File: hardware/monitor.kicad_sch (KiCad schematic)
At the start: 1 part, among them U36 Teensy++2.0

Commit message: Snapshot ep 24 work
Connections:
- net ~{A16} renamed A16
- net ~{A17} renamed A17
- net ~{A18} renamed A18
- net ~{A19} renamed A19
- net ~{A20} renamed A20
- net ~{A21} renamed A21
- net ~{A22} renamed A22
- net ~{A23} renamed A23
- net ~{CLK_EN} renamed ~{CLK_EN_OUT}
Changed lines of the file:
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@@
   (title_block
     (title "Monitor Module")
-    (date "2022-05-23")
-    (rev "A.23")
+    (date "2022-07-04")
+    (rev "A.24")
     (comment 2 "https://github.com/adrienkohlbecker/65C816")
     (comment 3 "Licensed under CERN-OHL-W v2")
@@
     (stroke (width 0) (type default) (color 0 0 0 0))
   )
-  (wire (pts (xy 119.38 83.82) (xy 128.27 83.82))
+  (wire (pts (xy 113.03 83.82) (xy 128.27 83.82))
     (stroke (width 0) (type default) (color 0 0 0 0))
   )
@@
     (effects (font (size 1.27 1.27)) (justify right bottom))
   )
+  (label "A18" (at 175.26 76.2 180)
+    (effects (font (size 1.27 1.27)) (justify right bottom))
+  )
   (label "A3" (at 175.26 124.46 180)
     (effects (font (size 1.27 1.27)) (justify right bottom))
@@
     (effects (font (size 1.27 1.27)) (justify left bottom))
   )
-  (label "{ADDRESS}" (at 86.36 46.99 0)
+  (label "A[0..23]" (at 86.36 46.99 0)
     (effects (font (size 1.27 1.27)) (justify left bottom))
   )
@@
     (effects (font (size 1.27 1.27)) (justify right bottom))
   )
-  (label "~{A16}" (at 171.45 81.28 0)
-    (effects (font (size 1.27 1.27)) (justify left bottom))
-  )
-  (label "~{A20}" (at 171.45 71.12 0)
-    (effects (font (size 1.27 1.27)) (justify left bottom))
-  )
   (label "VA" (at 48.26 33.02 180)
     (effects (font (size 1.27 1.27)) (justify right bottom))
   )
-  (label "~{A23}" (at 121.92 66.04 0)
-    (effects (font (size 1.27 1.27)) (justify left bottom))
+  (label "A17" (at 175.26 78.74 180)
+    (effects (font (size 1.27 1.27)) (justify right bottom))
   )
   (label "D0" (at 121.92 93.98 0)
     (effects (font (size 1.27 1.27)) (justify left bottom))
   )
-  (label "~{A21}" (at 171.45 68.58 0)
-    (effects (font (size 1.27 1.27)) (justify left bottom))
+  (label "A16" (at 175.26 81.28 180)
+    (effects (font (size 1.27 1.27)) (justify right bottom))
   )
   (label "A1" (at 175.26 119.38 180)
     (effects (font (size 1.27 1.27)) (justify right bottom))
   )
-  (label "~{CLK_EN}" (at 52.07 25.4 0)
+  (label "A19" (at 175.26 73.66 180)
+    (effects (font (size 1.27 1.27)) (justify right bottom))
+  )
+  (label "~{CLK_EN_OUT}" (at 52.07 25.4 0)
     (effects (font (size 1.27 1.27)) (justify left bottom))
   )
@@
     (effects (font (size 1.27 1.27)) (justify left bottom))
   )
-  (label "~{CLK_EN}" (at 119.38 83.82 0)
+  (label "~{CLK_EN_OUT}" (at 113.03 83.82 0)
     (effects (font (size 1.27 1.27)) (justify left bottom))
   )
@@
     (effects (font (size 1.27 1.27)) (justify left bottom))
   )
-  (label "{ADDRESS}" (at 48.26 39.37 180)
+  (label "A[0..23]" (at 48.26 39.37 180)
     (effects (font (size 1.27 1.27)) (justify right bottom))
   )
@@
     (effects (font (size 1.27 1.27)) (justify left bottom))
   )
-  (label "~{A18}" (at 171.45 76.2 0)
-    (effects (font (size 1.27 1.27)) (justify left bottom))
-  )
   (label "A14" (at 171.45 109.22 0)
     (effects (font (size 1.27 1.27)) (justify left bottom))
   )
-  (label "SYNC" (at 121.92 91.44 0)
-    (effects (font (size 1.27 1.27)) (justify left bottom))
-  )
-  (label "~{A22}" (at 171.45 66.04 0)
-    (effects (font (size 1.27 1.27)) (justify left bottom))
+  (label "A22" (at 175.26 66.04 180)
+    (effects (font (size 1.27 1.27)) (justify right bottom))
   )
-  (label "~{A19}" (at 171.45 73.66 0)
+  (label "SYNC" (at 121.92 91.44 0)
     (effects (font (size 1.27 1.27)) (justify left bottom))
   )
@@
     (effects (font (size 1.27 1.27)) (justify left bottom))
   )
+  (label "A21" (at 175.26 68.58 180)
+    (effects (font (size 1.27 1.27)) (justify right bottom))
+  )
   (label "CLK_IN" (at 175.26 86.36 180)
     (effects (font (size 1.27 1.27)) (justify right bottom))
@@
     (effects (font (size 1.27 1.27)) (justify left bottom))
   )
+  (label "A23" (at 121.92 66.04 0)
+    (effects (font (size 1.27 1.27)) (justify left bottom))
+  )
   (label "D[0..7]" (at 86.36 133.35 0)
     (effects (font (size 1.27 1.27)) (justify left bottom))
@@
     (effects (font (size 1.27 1.27)) (justify right bottom))
   )
-  (label "~{A17}" (at 171.45 78.74 0)
-    (effects (font (size 1.27 1.27)) (justify left bottom))
+  (label "A20" (at 175.26 71.12 180)
+    (effects (font (size 1.27 1.27)) (justify right bottom))
   )
-  (hierarchical_label "~{CLK_EN}" (shape output) (at 67.31 25.4 0)
+  (hierarchical_label "~{CLK_EN_OUT}" (shape output) (at 67.31 25.4 0)
     (effects (font (size 1.27 1.27)) (justify left))
   )
@@
     (effects (font (size 1.27 1.27)) (justify right))
   )
-  (hierarchical_label "{ADDRESS}" (shape input) (at 33.02 39.37 180)
+  (hierarchical_label "A[0..23]" (shape input) (at 33.02 39.37 180)
     (effects (font (size 1.27 1.27)) (justify right))
   )
@@
       (effects (font (size 1.524 1.524)) (justify left) hide)
     )
-    (property "Datasheet" "" (id 3) (at 148.59 114.3 0)
-      (effects (font (size 1.524 1.524)))
+    (property "Datasheet" "https://www.pjrc.com/store/teensypp.html" (id 3) (at 148.59 114.3 0)
+      (effects (font (size 1.524 1.524)) hide)
     )
     (pin "1")

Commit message: More updates
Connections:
- net CLK_IN renamed CLK_SRC

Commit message: Updates for episode 25
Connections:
- net CLK_SRC renamed CLK_IN
- net ~{CLK_EN_OUT} renamed ~{CLK_EN}
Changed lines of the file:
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@@
   (title_block
     (title "Monitor Module")
-    (date "2022-07-04")
-    (rev "A.24")
+    (date "2022-07-28")
+    (rev "A.25")
     (comment 2 "https://github.com/adrienkohlbecker/65C816")
     (comment 3 "Licensed under CERN-OHL-W v2")
@@
     (stroke (width 0) (type default) (color 0 0 0 0))
   )
-  (wire (pts (xy 113.03 83.82) (xy 128.27 83.82))
+  (wire (pts (xy 119.38 83.82) (xy 128.27 83.82))
     (stroke (width 0) (type default) (color 0 0 0 0))
   )
@@
     (effects (font (size 1.27 1.27)) (justify right bottom))
   )
-  (label "~{CLK_EN_OUT}" (at 52.07 25.4 0)
+  (label "~{CLK_EN}" (at 52.07 25.4 0)
     (effects (font (size 1.27 1.27)) (justify left bottom))
   )
@@
     (effects (font (size 1.27 1.27)) (justify left bottom))
   )
-  (label "~{CLK_EN_OUT}" (at 113.03 83.82 0)
+  (label "~{CLK_EN}" (at 119.38 83.82 0)
     (effects (font (size 1.27 1.27)) (justify left bottom))
   )
@@
     (effects (font (size 1.27 1.27)) (justify right bottom))
   )
-  (label "CLK_SRC" (at 52.07 29.21 0)
+  (label "CLK_IN" (at 52.07 29.21 0)
     (effects (font (size 1.27 1.27)) (justify left bottom))
   )
@@
     (effects (font (size 1.27 1.27)) (justify right bottom))
   )
-  (label "CLK_SRC" (at 177.8 86.36 180)
+  (label "CLK_IN" (at 177.8 86.36 180)
     (effects (font (size 1.27 1.27)) (justify right bottom))
   )
@@
     (effects (font (size 1.27 1.27)) (justify right bottom))
   )
-  (hierarchical_label "~{CLK_EN_OUT}" (shape output) (at 67.31 25.4 0)
+  (hierarchical_label "~{CLK_EN}" (shape output) (at 67.31 25.4 0)
     (effects (font (size 1.27 1.27)) (justify left))
   )
@@
     (effects (font (size 1.27 1.27)) (justify right))
   )
-  (hierarchical_label "CLK_SRC" (shape bidirectional) (at 67.31 29.21 0)
+  (hierarchical_label "CLK_IN" (shape bidirectional) (at 67.31 29.21 0)
     (effects (font (size 1.27 1.27)) (justify left))
   )

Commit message: Update main project
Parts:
- renumbered U36 to U25
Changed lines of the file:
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@@
   (symbol (lib_id "power:GND") (at 184.15 88.9 0) (unit 1)
     (in_bom yes) (on_board yes) (fields_autoplaced)
-    (property "Reference" "#PWR0125" (id 0) (at 184.15 95.25 0)
+    (property "Reference" "#PWR093" (id 0) (at 184.15 95.25 0)
       (effects (font (size 1.27 1.27)) hide)
     )
@@
   (symbol (lib_id "65C816:Teensy++2.0") (at 146.05 97.79 0) (unit 1)
     (in_bom yes) (on_board yes)
-    (property "Reference" "U36" (id 0) (at 133.35 58.42 0)
+    (property "Reference" "U25" (id 0) (at 133.35 58.42 0)
       (effects (font (size 1.524 1.524)) (justify left))
     )
@@
   (symbol (lib_id "power:GND") (at 115.57 63.5 0) (unit 1)
     (in_bom yes) (on_board yes) (fields_autoplaced)
-    (property "Reference" "#PWR0124" (id 0) (at 115.57 69.85 0)
+    (property "Reference" "#PWR092" (id 0) (at 115.57 69.85 0)
       (effects (font (size 1.27 1.27)) hide)
     )

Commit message: Episode 25
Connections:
- net CLK_IN renamed CLK_SRC
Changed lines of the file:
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@@
     (effects (font (size 1.27 1.27)) (justify right bottom))
   )
-  (label "CLK_IN" (at 52.07 29.21 0)
+  (label "CLK_SRC" (at 52.07 29.21 0)
     (effects (font (size 1.27 1.27)) (justify left bottom))
   )
@@
     (effects (font (size 1.27 1.27)) (justify right bottom))
   )
-  (label "CLK_IN" (at 177.8 86.36 180)
+  (label "CLK_SRC" (at 177.8 86.36 180)
     (effects (font (size 1.27 1.27)) (justify right bottom))
   )
@@
     (effects (font (size 1.27 1.27)) (justify right))
   )
-  (hierarchical_label "CLK_IN" (shape bidirectional) (at 67.31 29.21 0)
+  (hierarchical_label "CLK_SRC" (shape bidirectional) (at 67.31 29.21 0)
     (effects (font (size 1.27 1.27)) (justify left))
   )

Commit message: Prep ep 28
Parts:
- added D2: 1N5819, Diode_THT:D_DO-41_SOD81_P10.16mm_Horizontal, symbol Diode:1N5819
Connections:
- net ~{ROM_WE}: now reaches U25.10 (D7_7)
- net BE: now reaches U25.7 (D4_4)
- net at U25.8 (D5_5): now also D2.1 (K)
- new net ~{MR}⎒: D2.2 (A)
- no-connect marks 9 -> 6

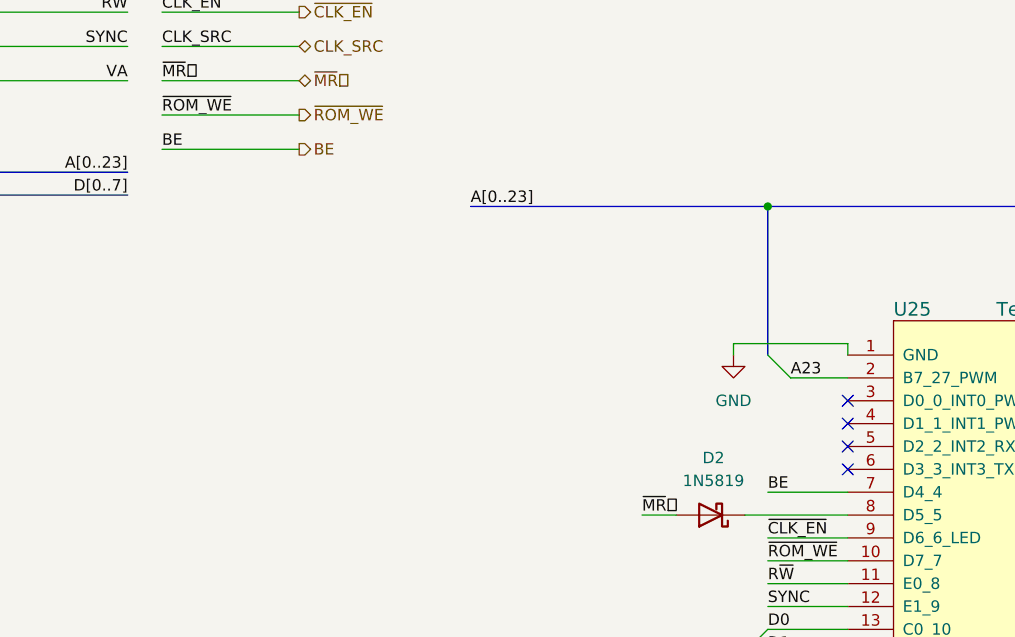
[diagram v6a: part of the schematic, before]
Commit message: Implement data polling
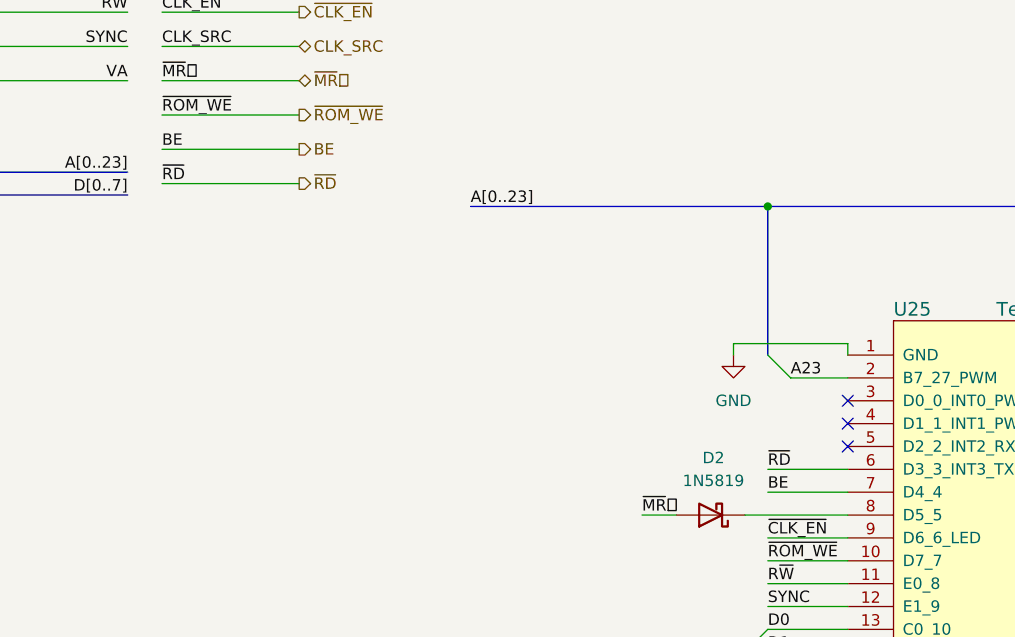
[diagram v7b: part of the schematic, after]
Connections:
- net ~{RD}: now reaches U25.6 (D3_3_INT3_TX)
- no-connect marks 6 -> 5
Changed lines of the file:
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@@
   (no_connect (at 128.27 71.12))
   (no_connect (at 128.27 73.66))
-  (no_connect (at 128.27 76.2))
   (no_connect (at 167.64 91.44))
   (no_connect (at 167.64 63.5))
@@
     (stroke (width 0) (type default) (color 0 0 0 0))
   )
+  (wire (pts (xy 119.38 76.2) (xy 128.27 76.2))
+    (stroke (width 0) (type default) (color 0 0 0 0))
+  )
   (wire (pts (xy 119.38 96.52) (xy 128.27 96.52))
     (stroke (width 0) (type default) (color 0 0 0 0))
@@
     (stroke (width 0) (type default) (color 0 0 0 0))
   )
+  (wire (pts (xy 67.31 44.45) (xy 52.07 44.45))
+    (stroke (width 0) (type default) (color 0 0 0 0))
+  )
   (wire (pts (xy 119.38 83.82) (xy 128.27 83.82))
     (stroke (width 0) (type default) (color 0 0 0 0))
@@
     (effects (font (size 1.27 1.27)) (justify left bottom))
   )
+  (label "~{RD}" (at 119.38 76.2 0)
+    (effects (font (size 1.27 1.27)) (justify left bottom))
+  )
   (label "A17" (at 177.8 78.74 180)
     (effects (font (size 1.27 1.27)) (justify right bottom))
@@
     (effects (font (size 1.27 1.27)) (justify right bottom))
   )
+  (label "~{RD}" (at 52.07 44.45 0)
+    (effects (font (size 1.27 1.27)) (justify left bottom))
+  )
   (label "A7" (at 177.8 134.62 180)
     (effects (font (size 1.27 1.27)) (justify right bottom))
@@
     (effects (font (size 1.27 1.27)) (justify left))
   )
+  (hierarchical_label "~{RD}" (shape output) (at 67.31 44.45 0)
+    (effects (font (size 1.27 1.27)) (justify left))
+  )
